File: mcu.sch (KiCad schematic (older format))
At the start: 101 parts, among them J3 SWD, J4 USB_B, J5 USB_EXT, J6 Micro_SD_Card_Det, J7 HC-05, Q1 AO3401A, U10 USBLC6-2SC6, U11 MCP2551-I-SN, U12 STM32F429ZGTx, U16 ATECC608A-SSHDA, U8 TPS5430DDA, U9 TPS5430DDA, Y1 25mhz, Y2 Crystal

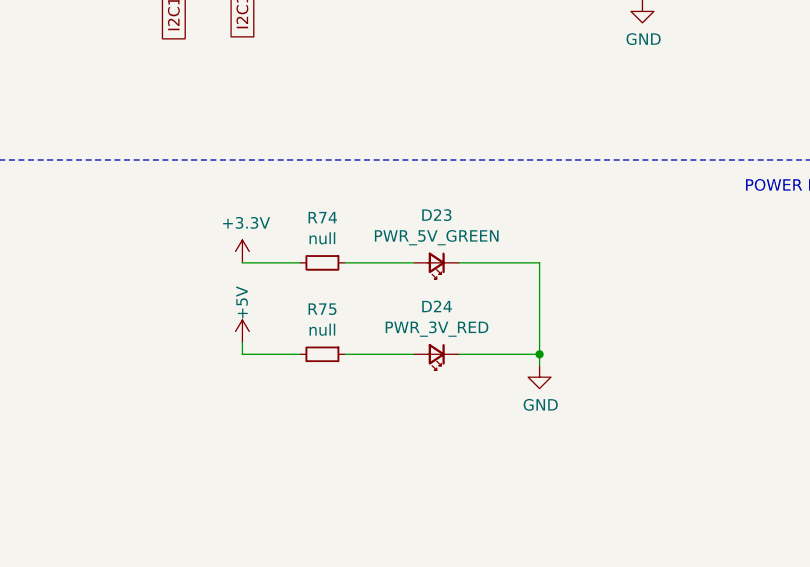
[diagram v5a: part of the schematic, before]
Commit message: Fixed LED names, added resistor values
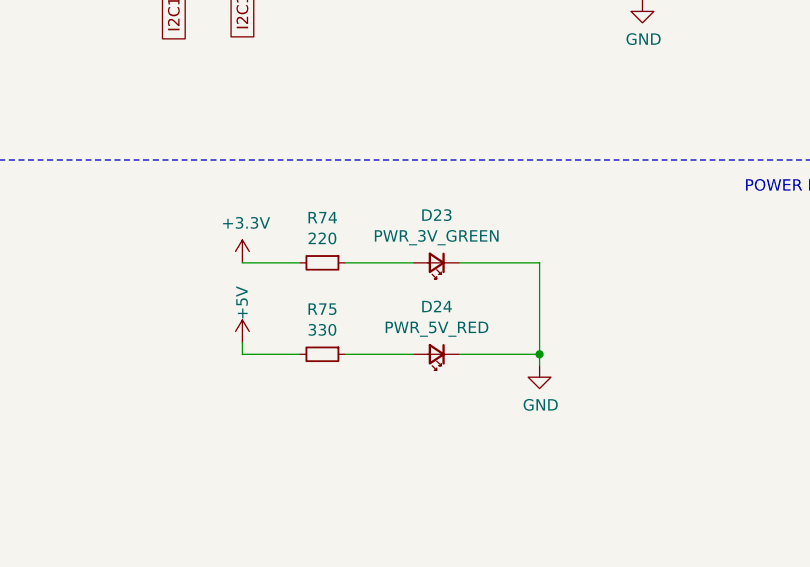
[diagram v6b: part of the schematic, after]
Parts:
- D23: value PWR_5V_GREEN -> PWR_3V_GREEN
- D24: value PWR_3V_RED -> PWR_5V_RED
- R74: value null -> 220
- R75: value null -> 330
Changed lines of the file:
@@
 P 14200 8750
 F 0 "D23" H 14200 8543 50  0000 C CNN
-F 1 "PWR_5V_GREEN" H 14200 8634 50  0000 C CNN
+F 1 "PWR_3V_GREEN" H 14200 8634 50  0000 C CNN
 F 2 "LED_SMD:LED_0603_1608Metric_Pad1.05x0.95mm_HandSolder" V 14200 8750 50  0001 C CNN
 F 3 "https://datasheet.lcsc.com/lcsc/1912111437_TOGIALED-TJ-S1608CY6T5ALC2G-A5_C440518.pdf" V 14200 8750 50  0001 C CNN
@@
 P 13700 8750
 F 0 "R74" V 13504 8750 50  0000 C CNN
-F 1 "null" V 13595 8750 50  0000 C CNN
+F 1 "220" V 13595 8750 50  0000 C CNN
 F 2 "Resistor_SMD:R_0603_1608Metric_Pad0.98x0.95mm_HandSolder" H 13700 8750 50  0001 C CNN
 F 3 "~" H 13700 8750 50  0001 C CNN
@@
 P 13700 9150
 F 0 "R75" V 13504 9150 50  0000 C CNN
-F 1 "null" V 13595 9150 50  0000 C CNN
+F 1 "330" V 13595 9150 50  0000 C CNN
 F 2 "Resistor_SMD:R_0603_1608Metric_Pad0.98x0.95mm_HandSolder" H 13700 9150 50  0001 C CNN
 F 3 "~" H 13700 9150 50  0001 C CNN
@@
 P 14200 9150
 F 0 "D24" H 14200 8943 50  0000 C CNN
-F 1 "PWR_3V_RED" H 14200 9034 50  0000 C CNN
+F 1 "PWR_5V_RED" H 14200 9034 50  0000 C CNN
 F 2 "LED_SMD:LED_0603_1608Metric_Pad1.05x0.95mm_HandSolder" V 14200 9150 50  0001 C CNN
 F 3 "https://datasheet.lcsc.com/lcsc/1811141223_TOGIALED-TJ-S1608SW6TGLC2R-A5_C192315.pdf" V 14200 9150 50  0001 C CNN

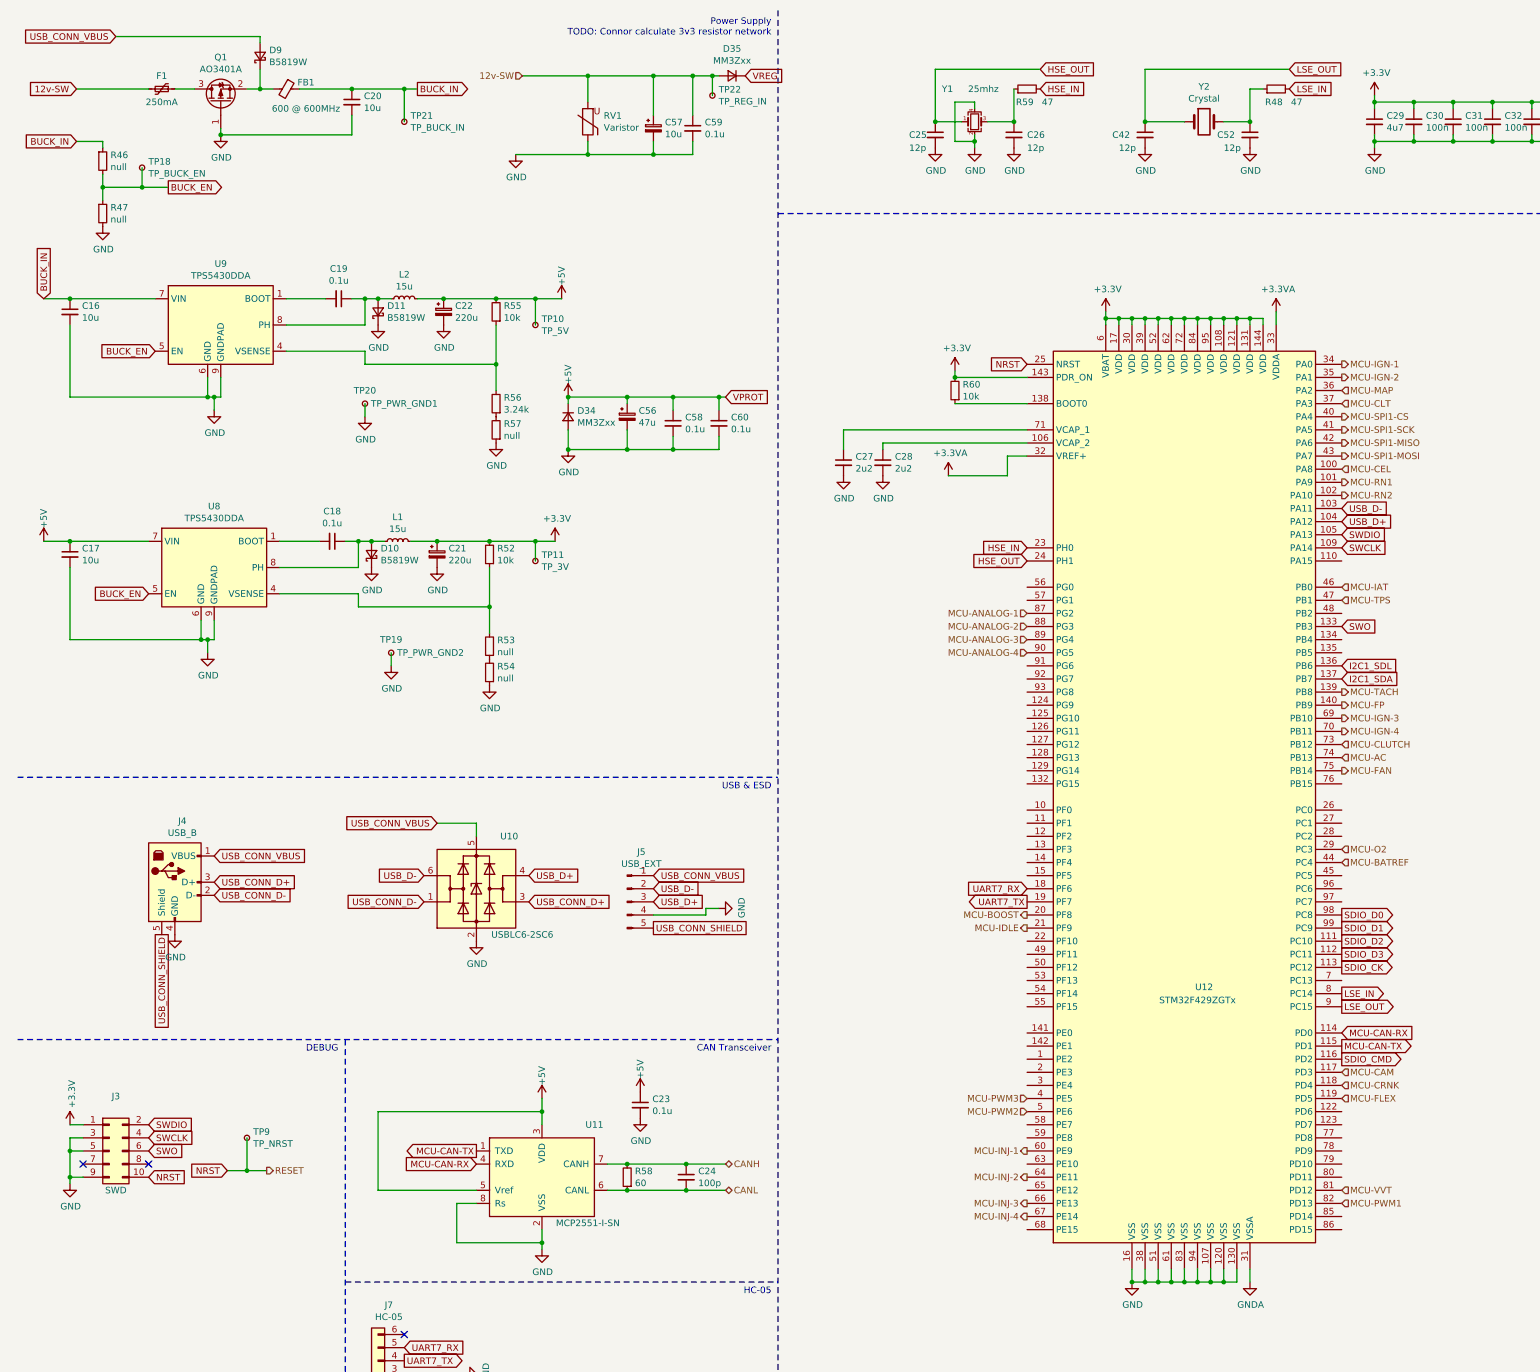
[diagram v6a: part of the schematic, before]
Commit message: Schematic and Layout Updates
* cleanup unused pins for DRC
* swap swd connector for the fancy one the phill uses
* swap out the CAN transciever for one more suitable for 3v3
* reroute CAN differential pair
* clean up copper pours
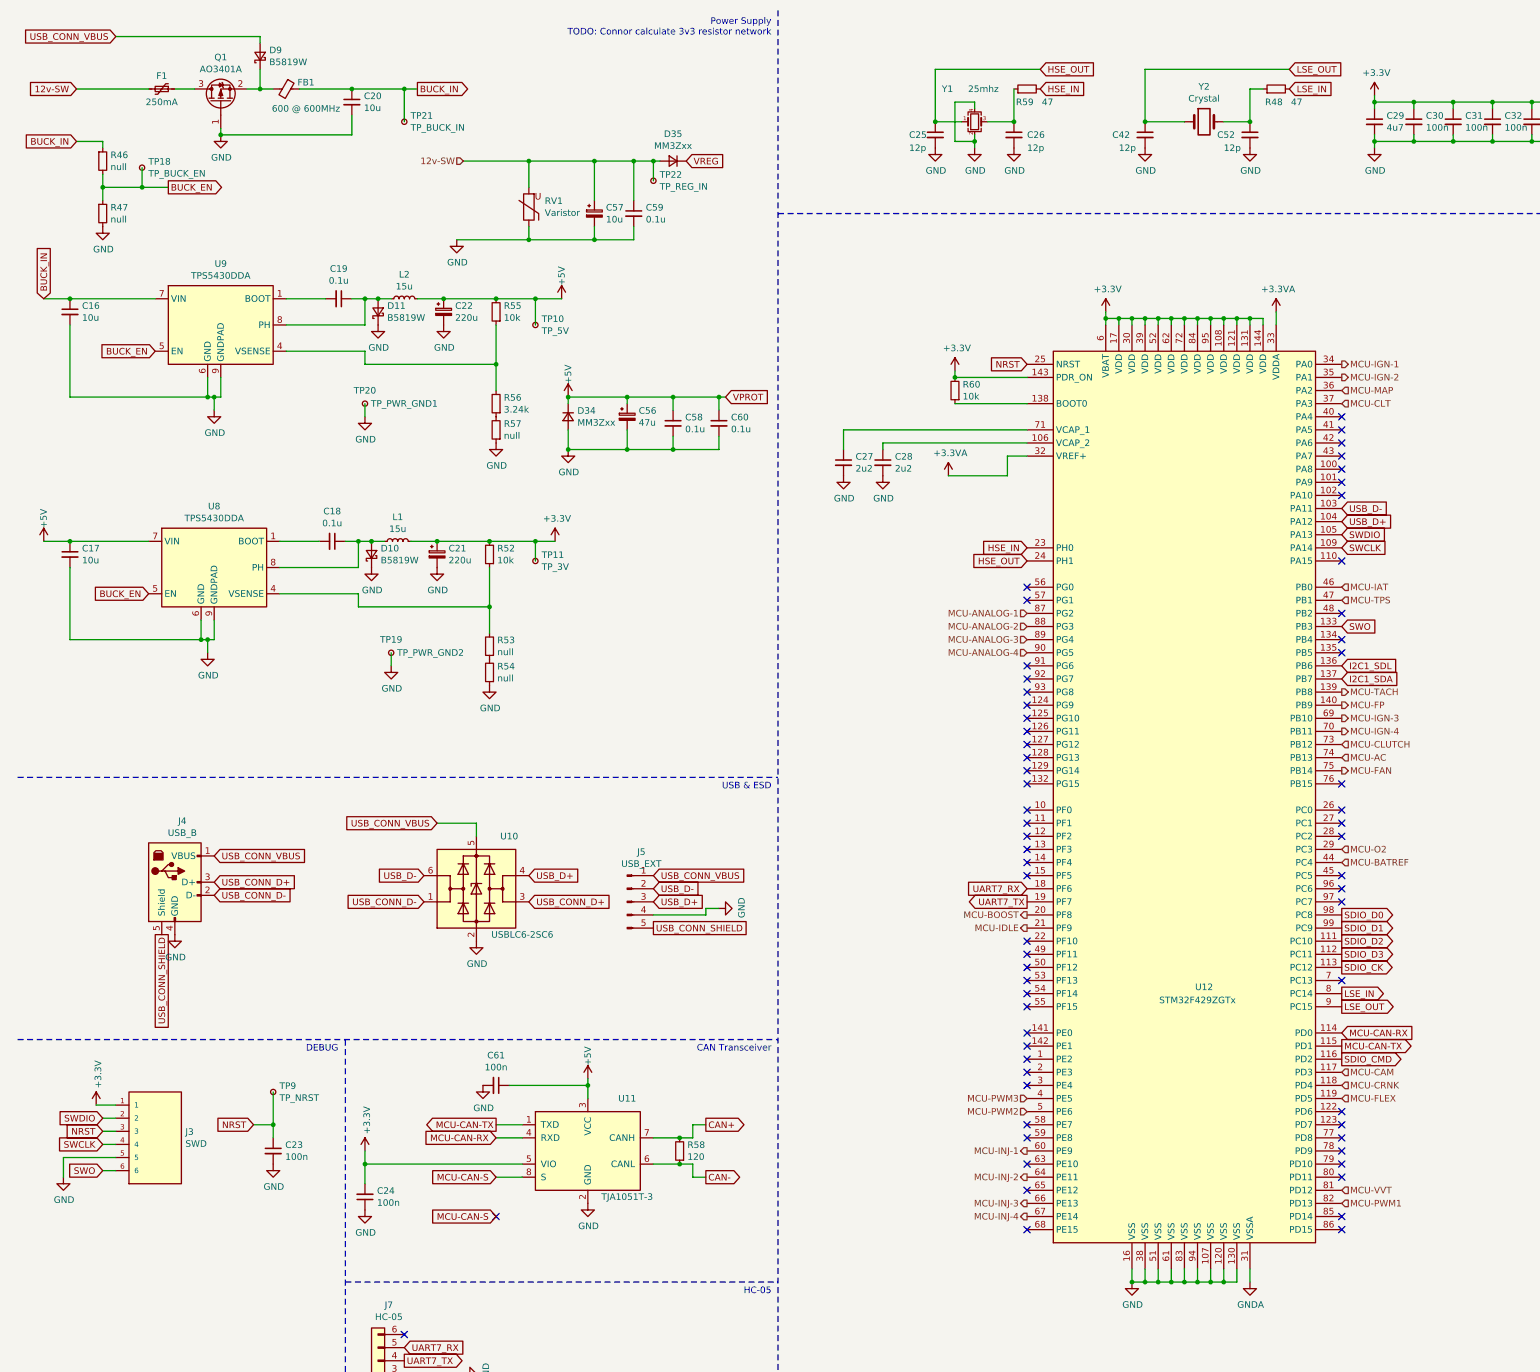
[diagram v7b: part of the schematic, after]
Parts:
- removed J3: SWD, Connector_PinSocket_1.27mm:PinSocket_2x05_P1.27mm_Vertical_SMD, symbol Connector_Generic:Conn_02x05_Odd_Even
- removed U11: MCP2551-I-SN, Package_SO:SOIC-8_3.9x4.9mm_P1.27mm, symbol Interface_CAN_LIN:MCP2551-I-SN
- added C61: 100n, Capacitor_SMD:C_0402_1005Metric_Pad0.74x0.62mm_HandSolder, symbol Device:C_Small
- added J3: SWD, TC2030-IDC-NL:TAG_TC2030-IDC-NL, symbol TC2030-IDC-NL:TC2030-IDC-NL
- added U11: TJA1051T-3, Package_SO:SOIC-8_3.9x4.9mm_P1.27mm, symbol Interface_CAN_LIN:TJA1051T-3
- C23: value 0.1u -> 100n
- C24: value 100p -> 100n
- R58: value 60 -> 120; footprint Resistor_SMD:R_0402_1005Metric_Pad0.72x0.64mm_HandSolder -> Resistor_SMD:R_0603_1608Metric_Pad0.98x0.95mm_HandSolder
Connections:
- net +3V3: now also C24.2, J3.1, U11.5 (VIO)
- net +5V: now also C61.1, U11.3 (VCC); no longer C23.1
- net GND: now also C24.1, C61.2, J3.5, U11.2 (GND)
- net MCU-CAN-RX: now also U11.4 (RXD)
- net MCU-CAN-TX: now also U11.1 (TXD)
- net NRST: now also C23.1, J3.3
- net SWCLK: now also J3.4
- net SWDIO: now also J3.2
- net SWO: now also J3.6
- net CANH renamed CAN+
- net CAN+: now also U11.7 (CANH); no longer C24.1
- net CANL renamed CAN-
- net CAN-: now also U11.6 (CANL); no longer C24.2
- net MCU-CEL: no longer names the net of U12.100 (PA8)
- net MCU-RN1: no longer names the net of U12.101 (PA9)
- net MCU-RN2: no longer names the net of U12.102 (PA10)
- net MCU-SPI1-CS: no longer names the net of U12.40 (PA4)
- net MCU-SPI1-MISO: no longer names the net of U12.42 (PA6)
- net MCU-SPI1-MOSI: no longer names the net of U12.43 (PA7)
- net MCU-SPI1-SCK: no longer names the net of U12.41 (PA5)
- new net MCU-CAN-S: U11.8 (S)
- no-connect marks 7 -> 67
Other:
- moved on the sheet: C57, C59, D35, RV1, TP22, TP9
